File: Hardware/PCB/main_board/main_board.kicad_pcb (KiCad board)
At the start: 2 copper layers, 150 x 177.5 mm, 65 parts, among them J1 SWD, J2 USB_A, J3 DIN-5_180degree, J4 USB_B, Q1 BC547, U1 MCP6002-xSN, U2 NUCLEO-F446RE, U3 6N137

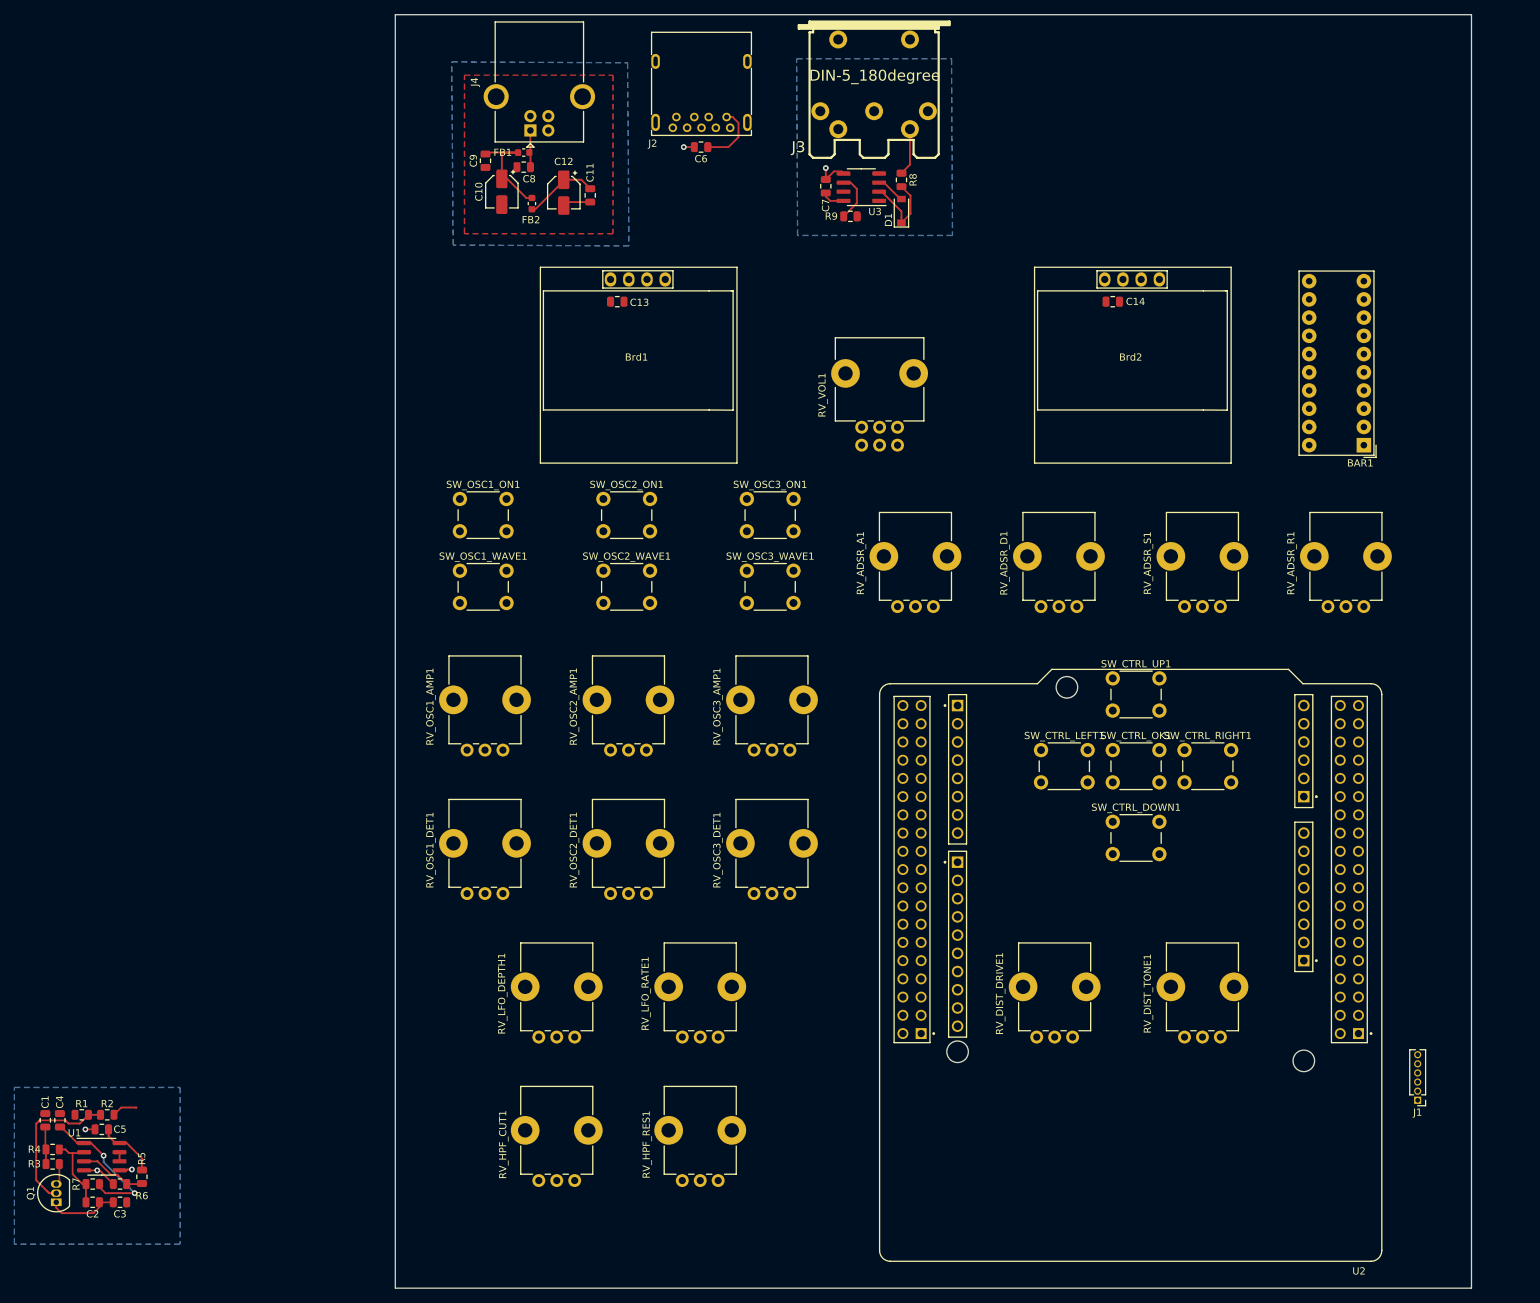
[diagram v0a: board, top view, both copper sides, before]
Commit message: Flip connectors, add 3D models
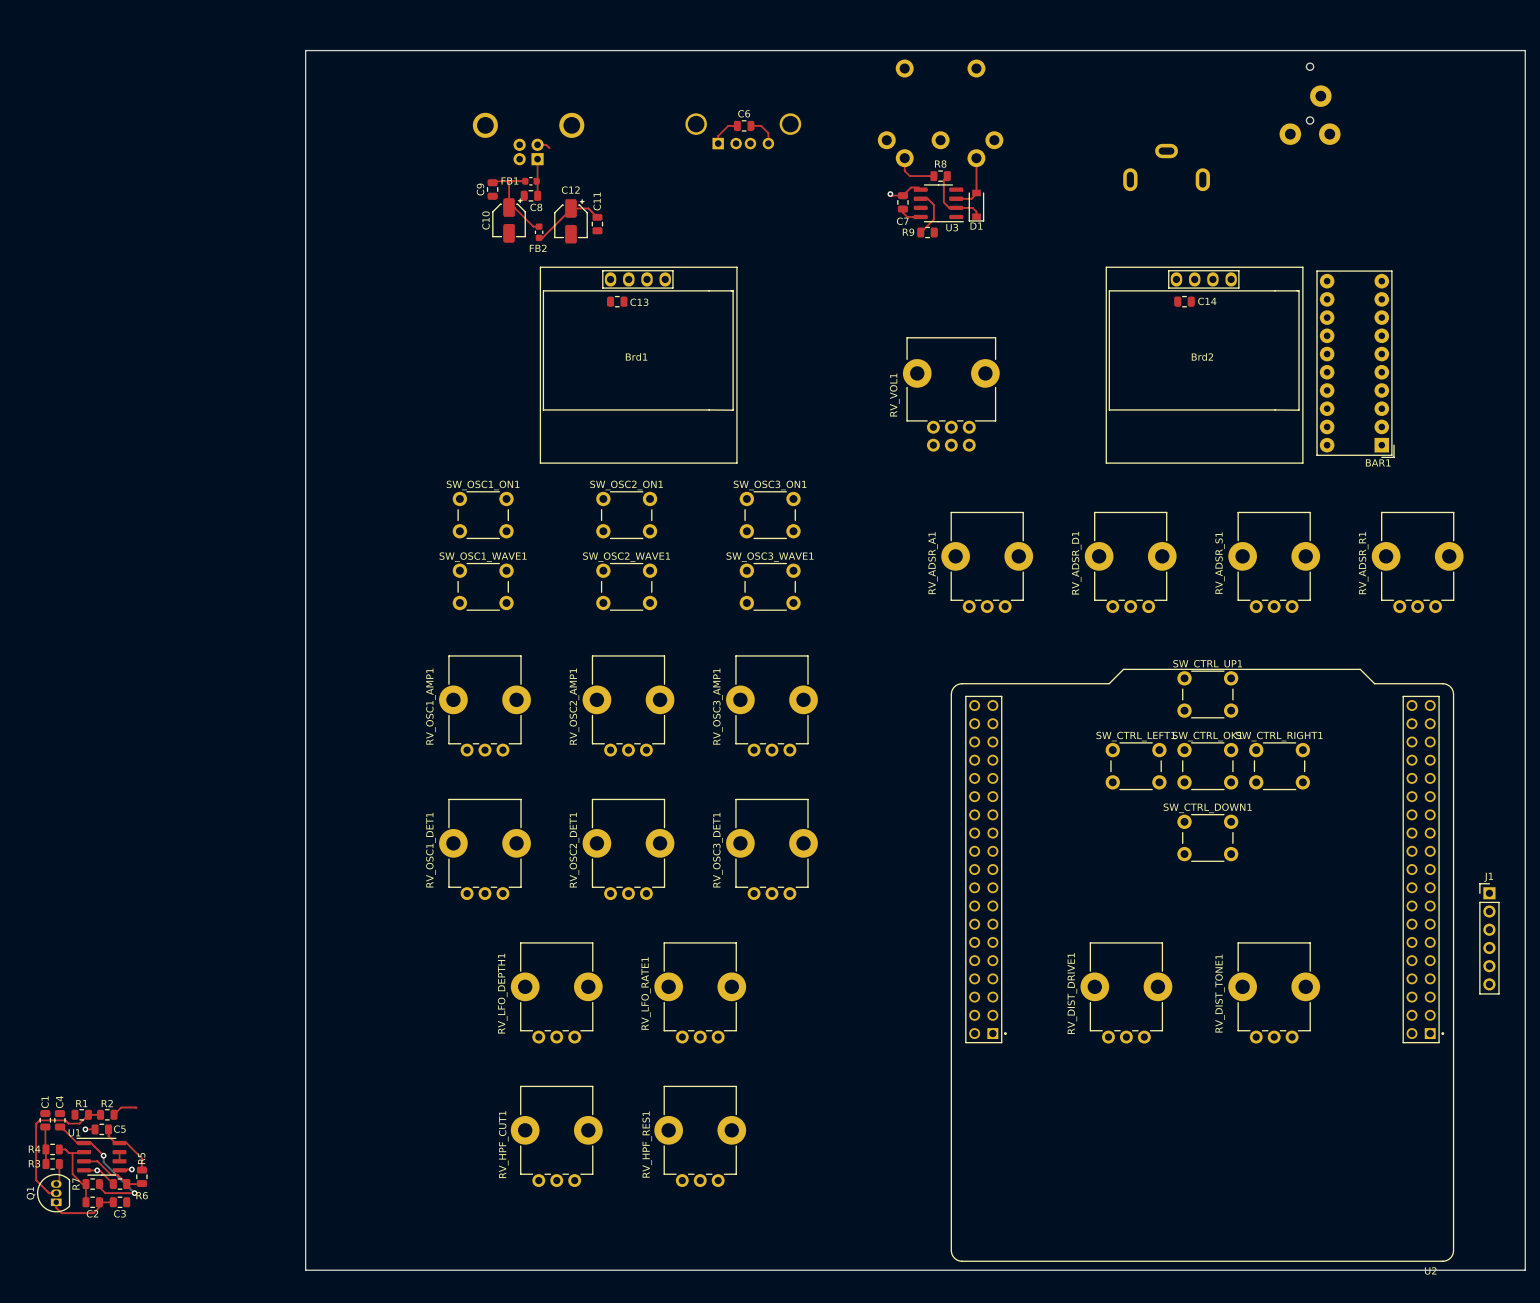
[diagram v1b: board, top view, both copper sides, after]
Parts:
- added J5: Conn_Coaxial, lib:rca_black, B.Cu at (130.0, 34.0)
- added J6: AudioJack3, lib:audio_jack_3.5mm_KYCON_STX-3000, B.Cu at (150.0, 18.2)
- J1: footprint Connector_PinHeader_1.27mm:PinHeader_1x06_P1.27mm_Vertical -> Connector_PinHeader_2.54mm:PinHeader_1x06_P2.54mm_Vertical
- J2: footprint Connector_USB:USB3_A_Molex_48393-001 -> Connector_USB:USB_A_Stewart_SS-52100-001_Horizontal; moved to B.Cu
- J3, J4: moved to B.Cu
- moved J1 30.5 mm to (175.0, 137.5), turned to 0 degrees
- moved C7 11.0 mm to (93.3, 41.2)
- moved R9 11.0 mm to (96.7, 45.4)
- moved U3 11.0 mm to (98.2, 41.3)
- moved D1 10.5 mm to (103.5, 41.5)
- moved J3 10.1 mm to (98.5, 29.5), turned to 0 degrees
- moved Brd2 10.0 mm to (135.0, 62.5)
- moved C14 10.0 mm to (132.5, 55.0)
- moved RV_ADSR_A1 10.0 mm to (107.5, 97.5)
- moved RV_ADSR_D1 10.0 mm to (127.5, 97.5)
- moved RV_ADSR_R1 10.0 mm to (167.5, 97.5)
- moved RV_ADSR_S1 10.0 mm to (147.5, 97.5)
- moved RV_DIST_DRIVE1 10.0 mm to (126.9, 157.5)
- moved RV_DIST_TONE1 10.0 mm to (147.5, 157.5)
- moved RV_VOL1 10.0 mm to (102.5, 72.5)
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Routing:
- net +5V: track 27.9 -> 23.4 mm
- net Net-(D1-Pad2): track 4.06 -> 8.09 mm
- net Net-(D1-Pad1): track 11.9 -> 9.65 mm
- net GND: track 21.5 -> 22.1 mm, vias 5 -> 4
- removed copper zone on B.Cu, net GND
- removed copper zone on F.Cu, net GND
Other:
- board size 150 x 177.5 mm -> 170 x 170 mm

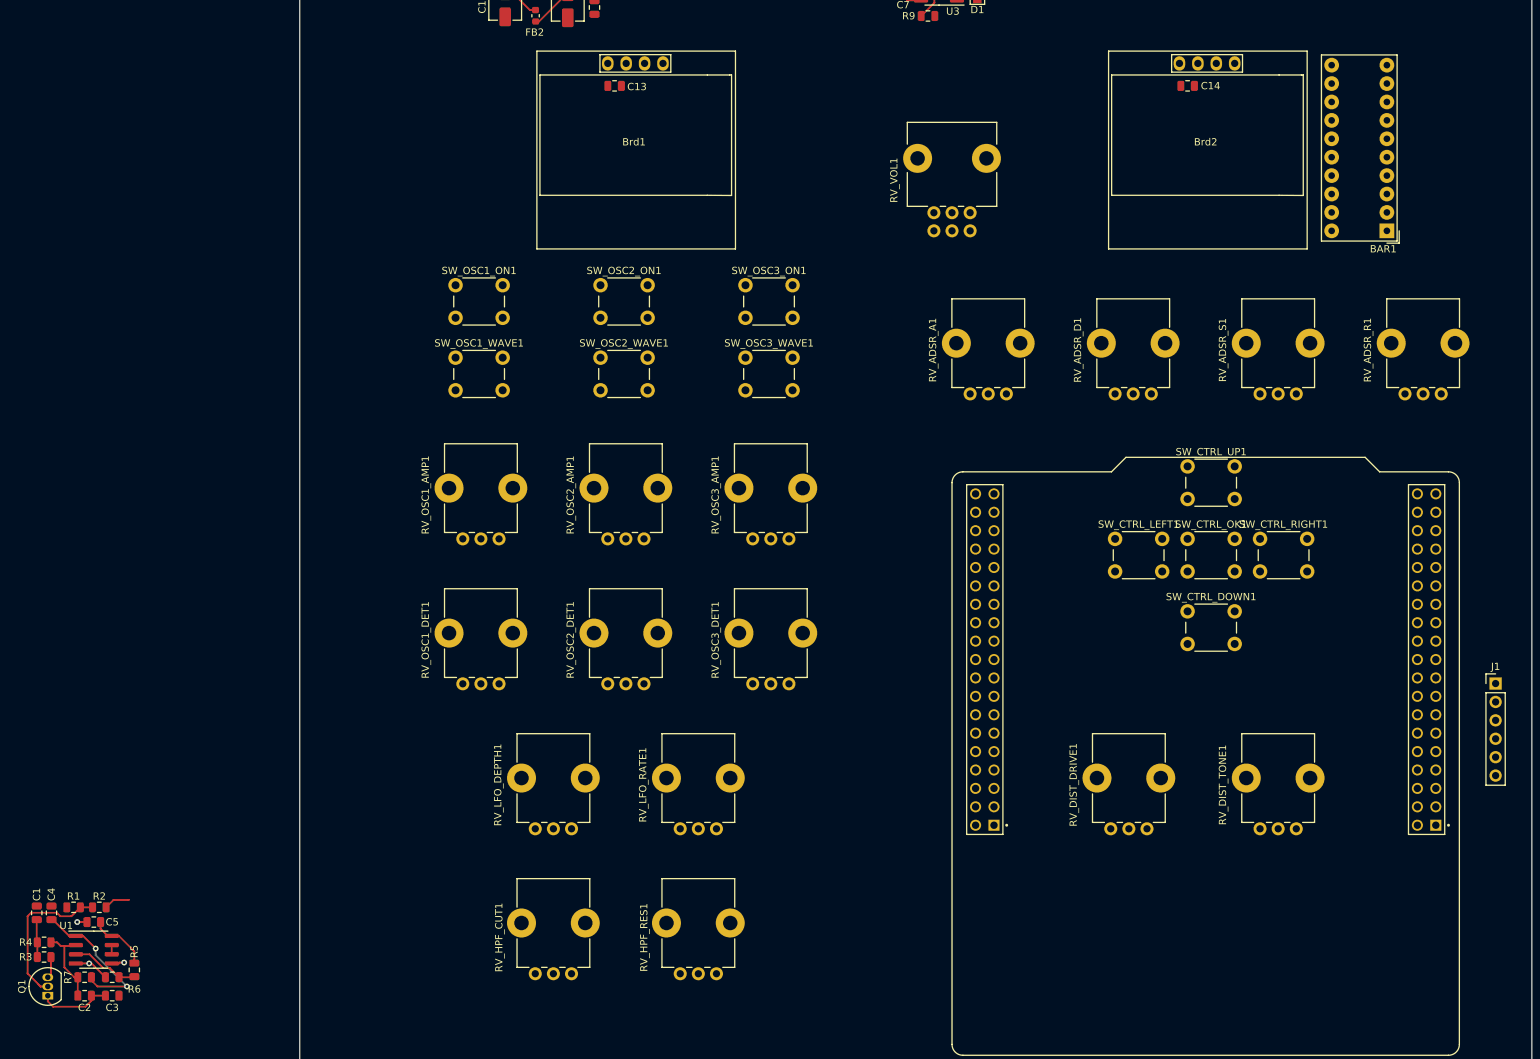
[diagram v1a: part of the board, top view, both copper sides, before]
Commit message: Place VCF components, I2C bus
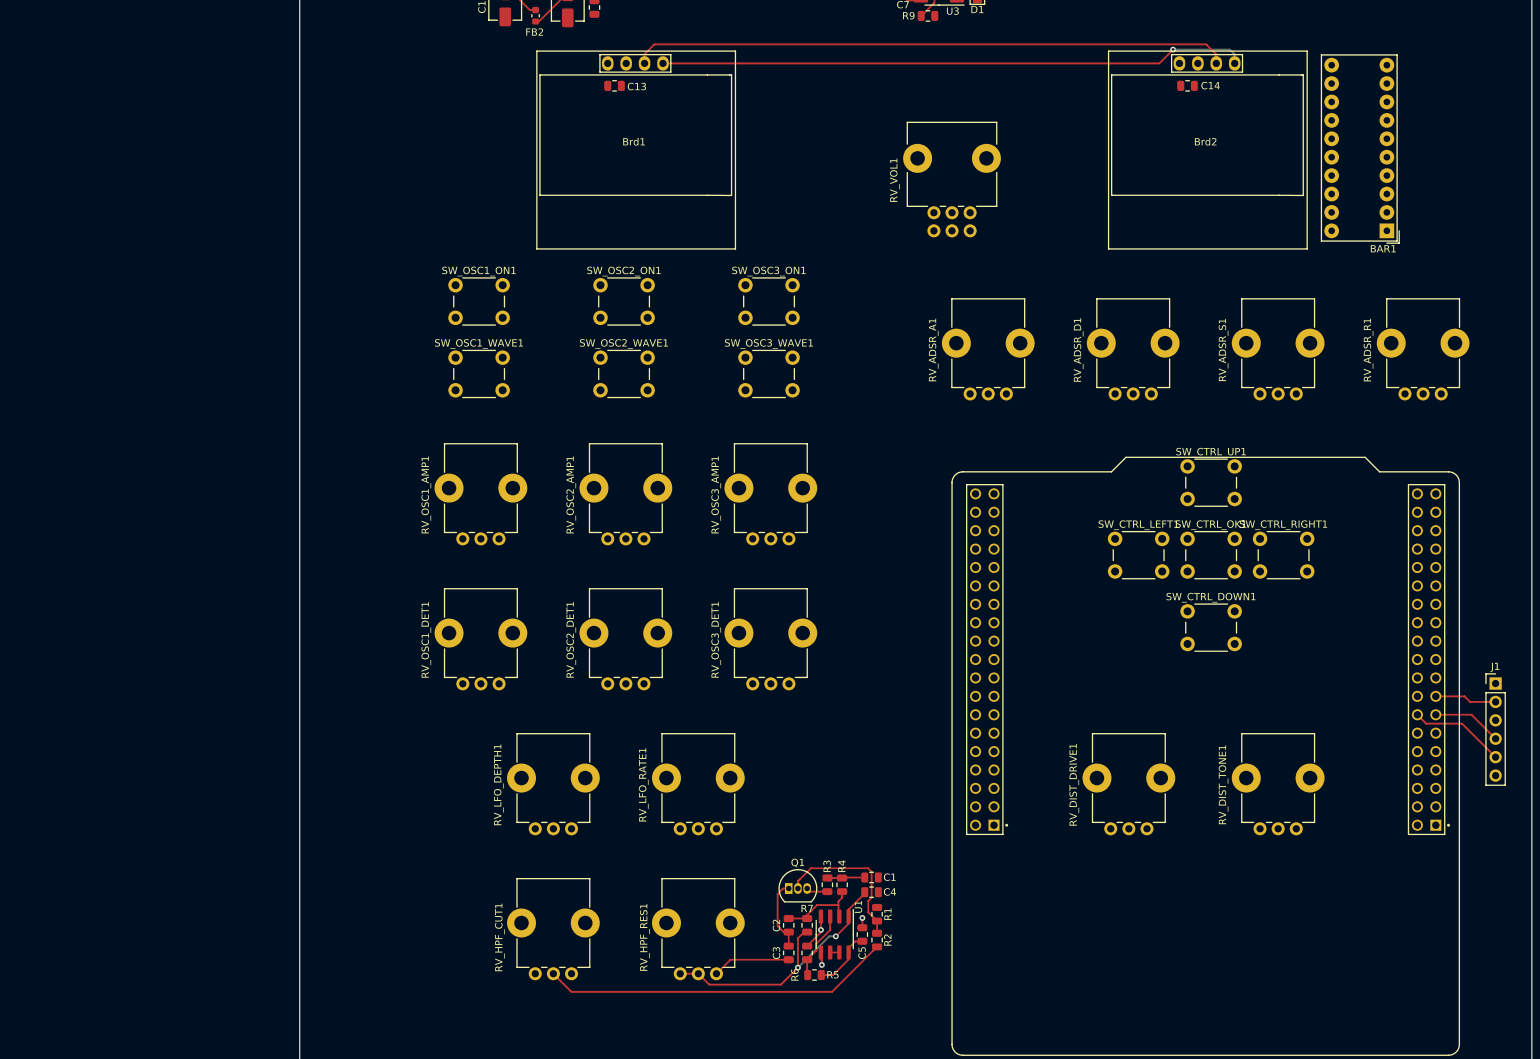
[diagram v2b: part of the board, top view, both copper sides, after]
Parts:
- moved C1 115.3 mm to (88.9, 164.2), turned to 0 degrees
- moved C4 113.2 mm to (88.9, 166.2), turned to 180 degrees
- moved R1 110.9 mm to (89.7, 169.3), turned to 90 degrees
- moved R4 110.4 mm to (84.8, 165.2), turned to 90 degrees
- moved R3 108.5 mm to (82.8, 165.2), turned to 90 degrees
- moved R2 107.4 mm to (89.7, 172.9), turned to 270 degrees
- moved C5 106.1 mm to (87.6, 172.1), turned to 270 degrees
- moved Q1 103.3 mm to (77.5, 165.7), turned to 0 degrees
- moved U1 102.3 mm to (83.8, 172.1), turned to 270 degrees
- moved R7 99.9 mm to (80.0, 170.8), turned to 90 degrees
- moved C2 97.6 mm to (77.5, 170.8), turned to 90 degrees
- moved R6 95.9 mm to (80.0, 174.6), turned to 90 degrees
- moved R5 93.9 mm to (81.0, 177.7), turned to 0 degrees
- moved C3 93.5 mm to (77.5, 174.6), turned to 90 degrees
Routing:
- net /HMI/I2C_display_SCL: track 0.00 -> 82.5 mm
- net /HMI/I2C_display_SDA: track 0.00 -> 81.2 mm, vias 0 -> 1
- net Net-(R2-Pad2): track 3.63 -> 48.3 mm
- net Net-(C4-Pad2): track 20.5 -> 38.3 mm
- net /MCU/NRST: track 0.00 -> 13.2 mm
- net Net-(C3-Pad1): track 0.00 -> 10.8 mm
- net /MCU/SWDIO: track 0.00 -> 9.62 mm
- net /MCU/SWCLK: track 0.00 -> 8.57 mm
